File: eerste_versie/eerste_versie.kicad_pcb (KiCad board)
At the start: 2 copper layers, 48.9 x 33.7 mm, 24 parts, among them J1 105017-1001, J2 Conn_01x02, U1 ESP32-WROOM-32U, U2 AMS1117-3.3

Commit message: feedback verbeterd
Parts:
- removed the G*** at (138.4, 120.7)
- added G***: LOGO, logo:biohazard_symbool_groter, B.Cu at (135.3, 120.7)
- Bat Connect: renamed from J2
- Prog head: renamed from Prog_head
- USB PWR: renamed from J1
- moved USB PWR 0.97 mm to (135.2, 136.9)
- renumbered SW to BAT/USB
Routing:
- net GND: track 77.6 -> 76.7 mm
- removed copper zone on F.Cu, net GND
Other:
- board text added: "+"
- board text added: "-"

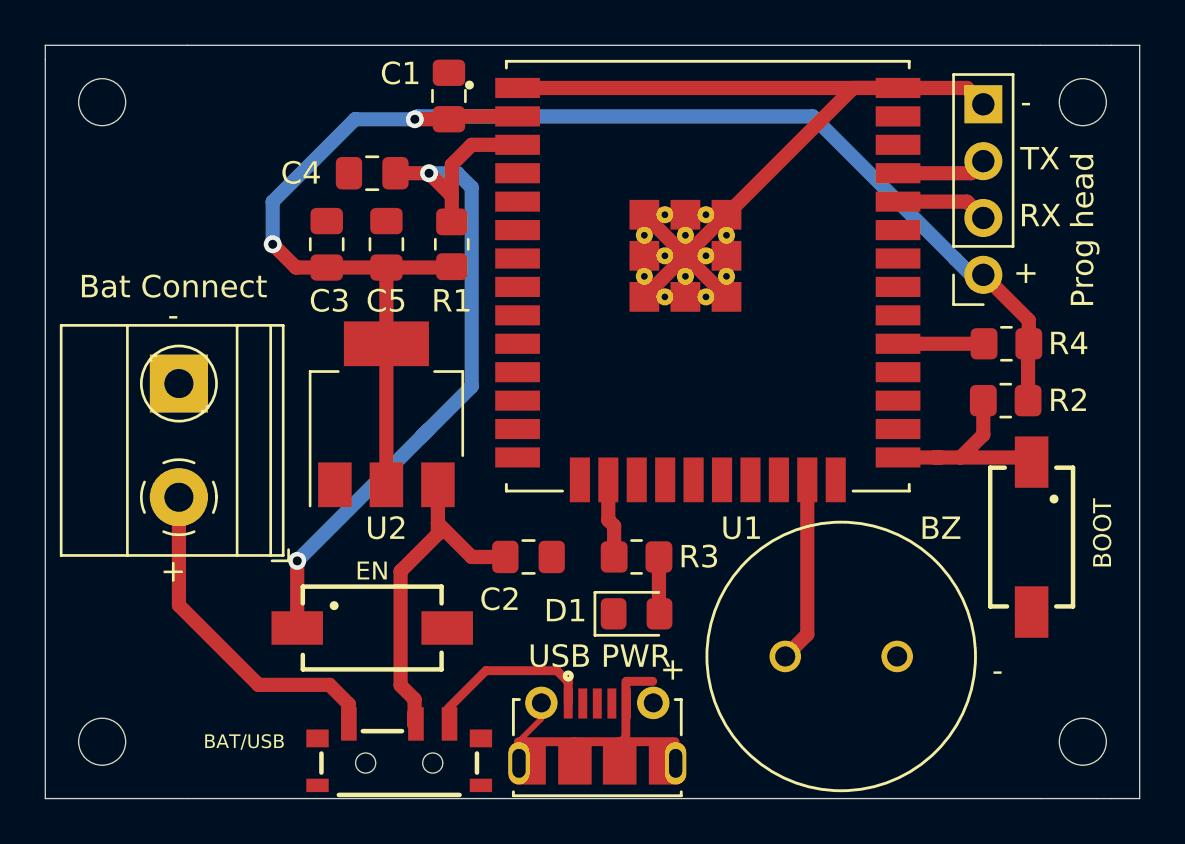
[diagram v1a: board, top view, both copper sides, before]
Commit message: grondvlak terug toegevoegd
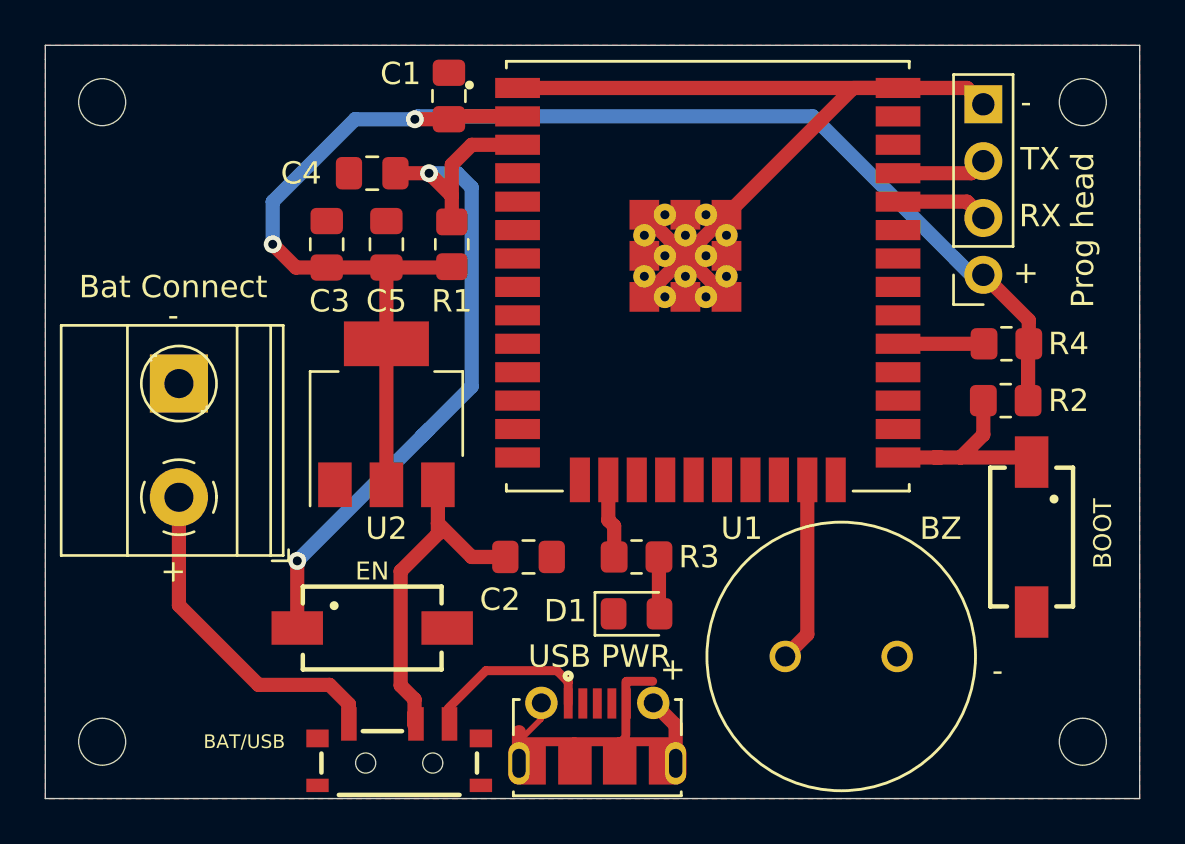
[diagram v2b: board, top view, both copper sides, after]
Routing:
- net GND: track 76.7 -> 82.2 mm
- added copper zone on F.Cu, net GND
